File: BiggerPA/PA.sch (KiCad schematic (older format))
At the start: 105 parts, among them J1 Conn_Coaxial, J10 Conn_01x01, J2 Conn_01x02, J27 Conn_01x01, J28 Conn_01x01, J3 Conn_Coaxial, J4 Conn_01x02, J5 Conn_01x02, J6 Conn_01x01, J7 Conn_01x01, J8 Conn_01x01, J9 Conn_01x01, Q1 2N3906, Q10 IRF510N, Q11 IRF510N, Q12 IRF510N, Q13 IRF510N, Q14 IRF510N, Q15 IRF510N, Q18 TIP42, Q19 TIP42, Q2 IRF510N, Q20 TIP42, Q3 IRF510N, Q4 2N3906, Q5 TIP42, Q6 IRF510N, Q7 IRF510N, Q8 IRF510N, Q9 IRF510N, T1 Transformer_1P1Sdotted, T2 Transformer_1P1Sdotted, T3 Transformer_1P1Sdotted

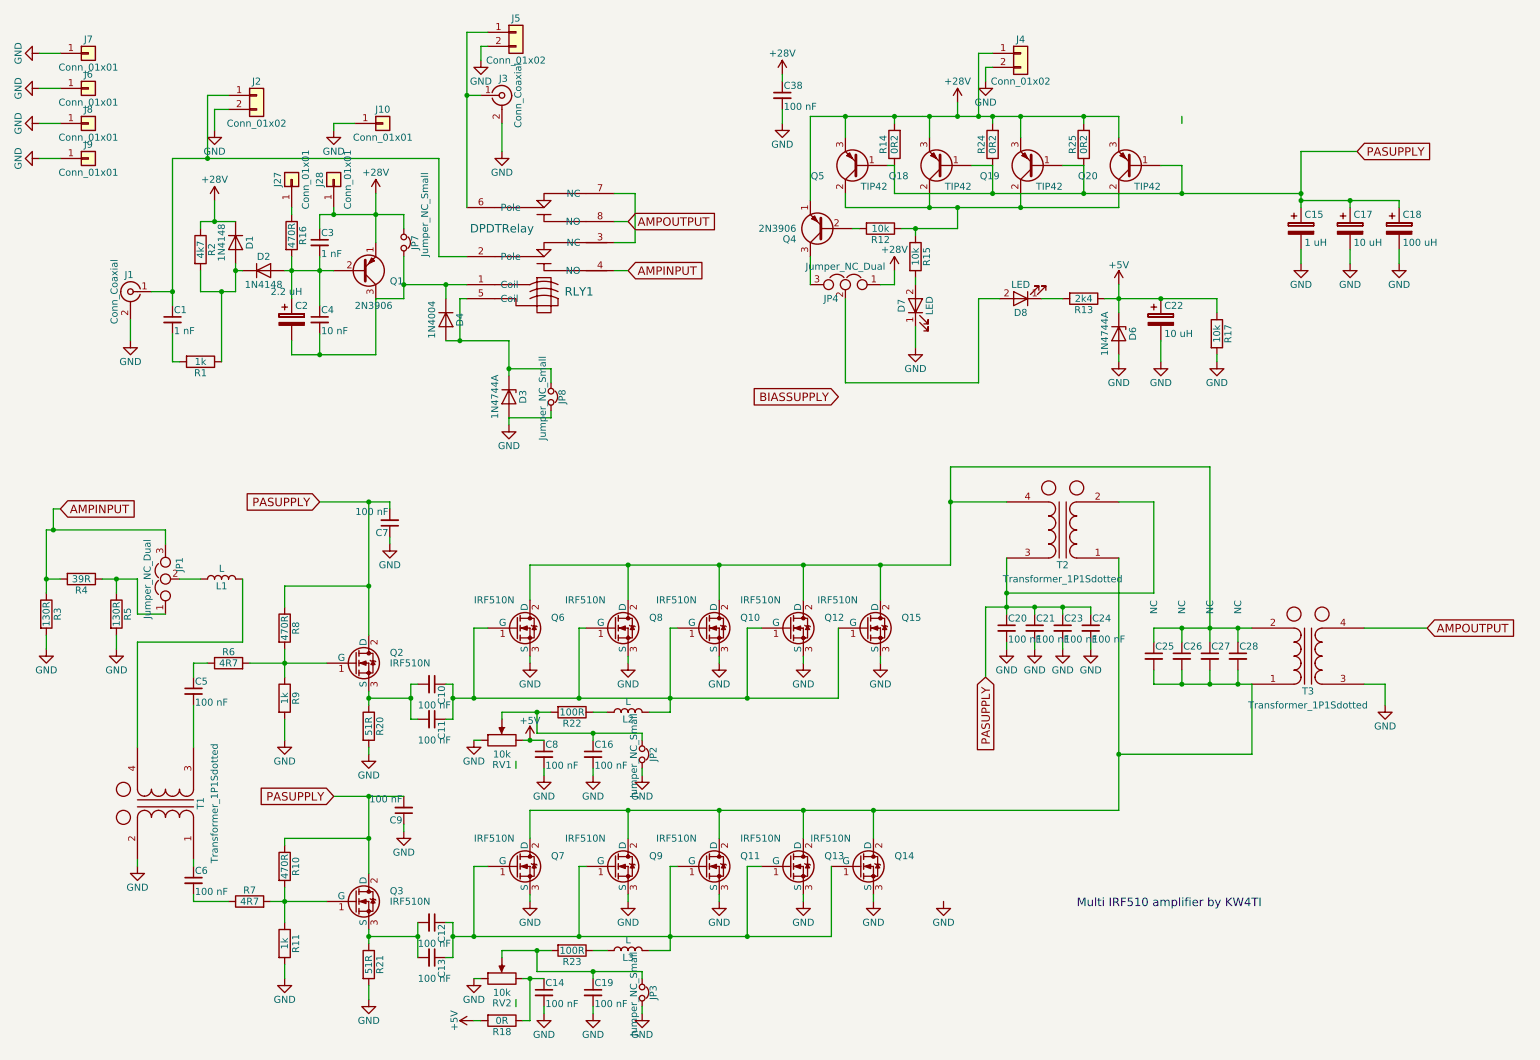
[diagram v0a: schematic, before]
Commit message: Added series inductor to gates
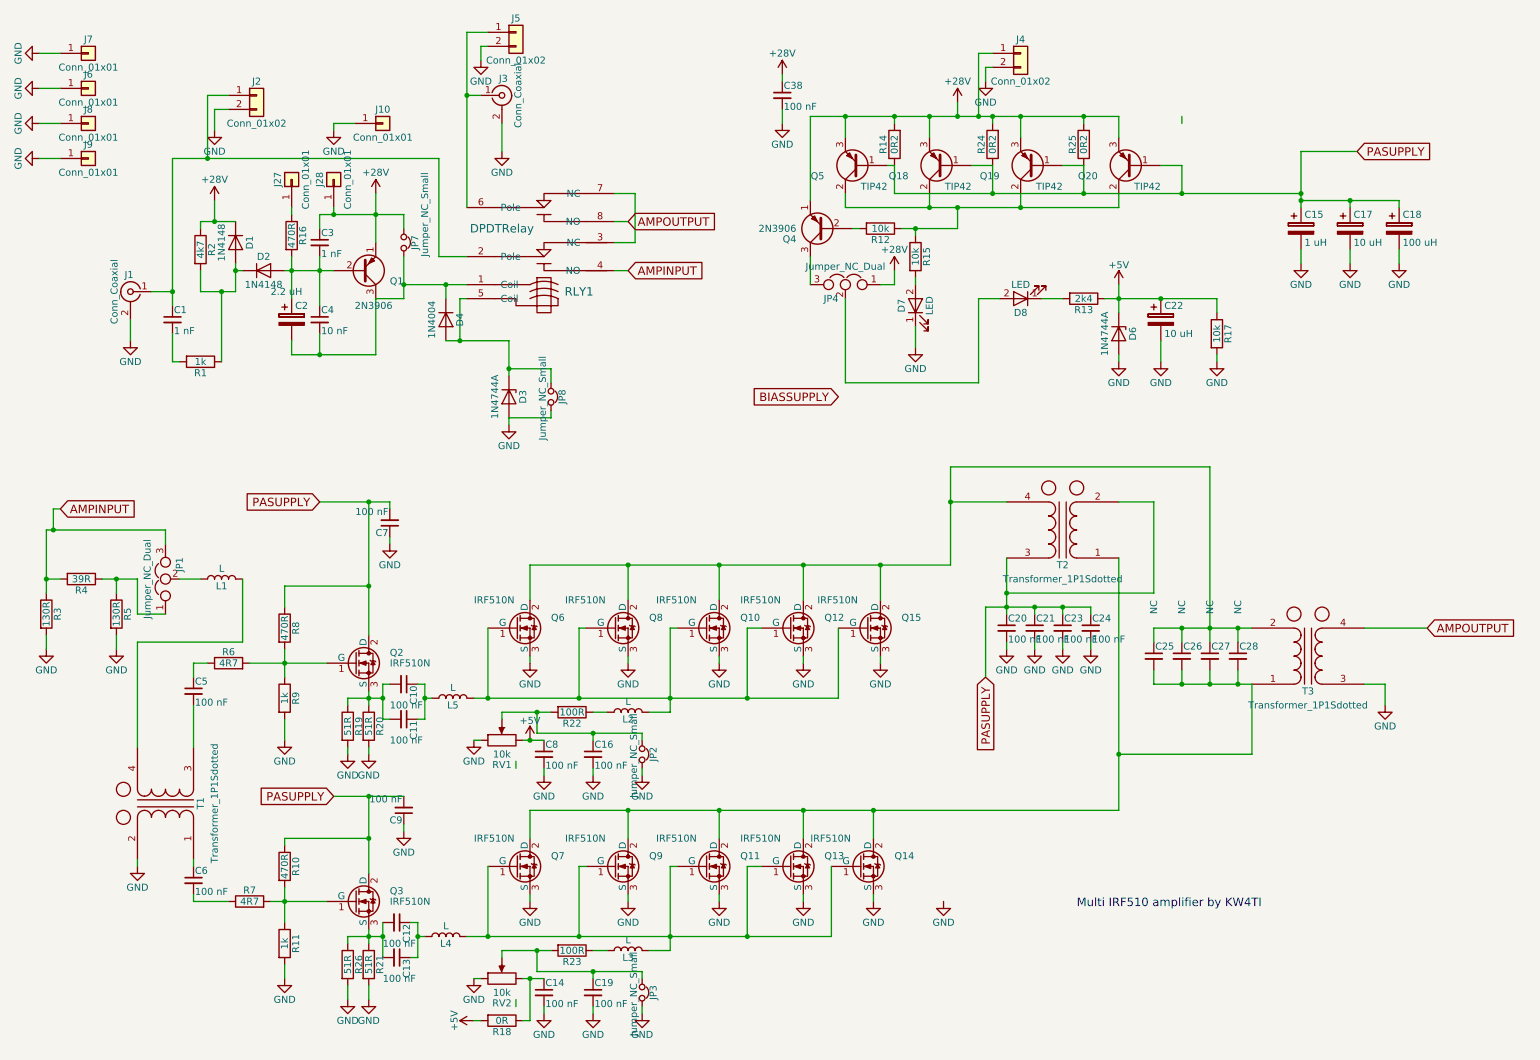
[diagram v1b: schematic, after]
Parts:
- added L4, L5: L, Inductors_THT:L_Axial_L6.6mm_D2.7mm_P10.16mm_Horizontal_Vishay_IM-2, symbol L
- added R19, R26: 51R, Resistors_THT:R_Axial_DIN0309_L9.0mm_D3.2mm_P12.70mm_Horizontal, symbol R
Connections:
- net GND: now also R19.2, R26.2
- net at C10.2, C11.2, Q2.3 (S)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: now also R19.1
- net at C12.2, C13.2, Q3.3 (S)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: now also R26.1
- net at L2.2, Q10.1 (G), Q12.1 (G)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: now also L5.2; no longer C10.1, C11.1
- net at L3.2, Q11.1 (G), Q13.1 (G)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: now also L4.2; no longer C12.1, C13.1
- new net: C10.1, C11.1, L5.1
- new net: C12.1, C13.1, L4.1
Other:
- moved on the sheet: C10, C11, C12, C13

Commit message: Added Filter
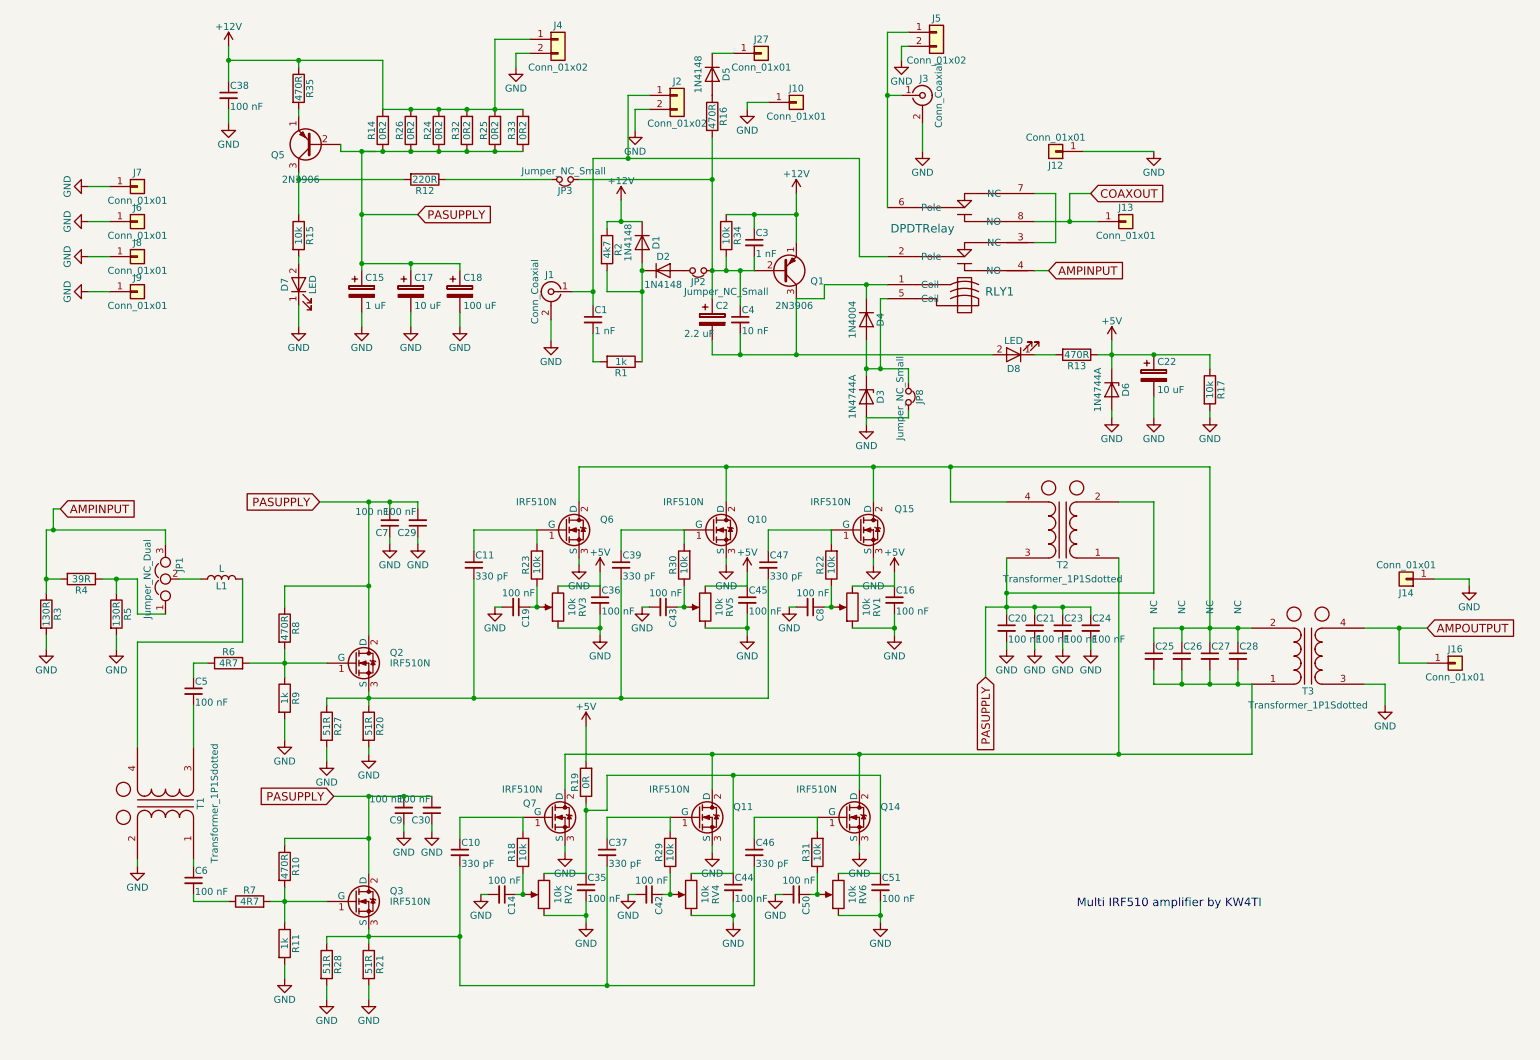
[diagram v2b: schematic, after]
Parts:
- removed C12, C13: 100 nF, Capacitors_THT:C_Disc_D5.0mm_W2.5mm_P5.00mm, symbol C_Small
- removed J28: Conn_01x01, Connectors:1pin, symbol Conn_01x01
- removed JP4: Jumper_NC_Dual, Pin_Headers:Pin_Header_Straight_1x03_Pitch2.54mm, symbol Jumper_NC_Dual
- removed JP7: Jumper_NC_Small, Pin_Headers:Pin_Header_Straight_1x02_Pitch2.54mm, symbol Jumper_NC_Small
- removed L2, L3, L4, L5: L, Inductors_THT:L_Axial_L6.6mm_D2.7mm_P10.16mm_Horizontal_Vishay_IM-2, symbol L
- removed Q12, Q13, Q8, Q9: IRF510N, PA:TO-220-3_Vertical_WithPads, symbol IRF540N
- removed Q18, Q19, Q20, Q5: TIP42, PA:TO-220-3_Vertical_WithPads, symbol TIP42
- removed Q4: 2N3906, TO_SOT_Packages_THT:TO-92_Molded_Narrow, symbol 2N3906
- added C29, C30, C35, C36, C42, C43, C44, C45, C50, C51: 100 nF, Capacitors_THT:C_Disc_D5.0mm_W2.5mm_P2.50mm, symbol C_Small
- added C37, C39, C46, C47: 330 pF, Capacitors_THT:C_Disc_D5.0mm_W2.5mm_P2.50mm, symbol C_Small
- added D5: 1N4148, Diodes_THT:D_DO-35_SOD27_P7.62mm_Horizontal, symbol D
- added J12, J13, J14, J16: Conn_01x01, Connectors:1pin, symbol Conn_01x01
- added Q5: 2N3906, TO_SOT_Packages_THT:TO-92_Molded_Narrow, symbol 2N3906
- added R27, R28: 51R, Resistors_THT:R_Axial_DIN0309_L9.0mm_D3.2mm_P12.70mm_Horizontal, symbol R
- added R29, R30, R31, R34: 10k, Resistors_THT:R_Axial_DIN0207_L6.3mm_D2.5mm_P7.62mm_Horizontal, symbol R
- added R32, R33: 0R2, Resistors_THT:R_Axial_DIN0411_L9.9mm_D3.6mm_P12.70mm_Horizontal, symbol R
- added R35: 470R, Resistors_THT:R_Axial_DIN0207_L6.3mm_D2.5mm_P7.62mm_Horizontal, symbol R
- added RV3, RV4, RV5, RV6: 10k, Potentiometers:Potentiometer_Trimmer_Bourns_3296W, symbol POT
- C10, C11: value 100 nF -> 330 pF; footprint Capacitors_THT:C_Disc_D5.0mm_W2.5mm_P5.00mm -> Capacitors_THT:C_Disc_D5.0mm_W2.5mm_P2.50mm
- C15: value 1 uH -> 1 uF
- C17, C22: value 10 uH -> 10 uF
- C18: value 100 uH -> 100 uF
- C2: value 2.2 uH -> 2.2 uF
- R12: value 10k -> 220R
- R13: value 2k4 -> 470R
- R18: value 0R -> 10k; footprint Resistors_THT:R_Axial_DIN0207_L6.3mm_D2.5mm_P10.16mm_Horizontal -> Resistors_THT:R_Axial_DIN0207_L6.3mm_D2.5mm_P7.62mm_Horizontal
- R19: value 51R -> 0R; footprint Resistors_THT:R_Axial_DIN0309_L9.0mm_D3.2mm_P12.70mm_Horizontal -> Resistors_THT:R_Axial_DIN0207_L6.3mm_D2.5mm_P7.62mm_Horizontal
- R22, R23: value 100R -> 10k; footprint Resistors_THT:R_Axial_DIN0207_L6.3mm_D2.5mm_P10.16mm_Horizontal -> Resistors_THT:R_Axial_DIN0207_L6.3mm_D2.5mm_P7.62mm_Horizontal
- R26: value 51R -> 0R2; footprint Resistors_THT:R_Axial_DIN0309_L9.0mm_D3.2mm_P12.70mm_Horizontal -> Resistors_THT:R_Axial_DIN0411_L9.9mm_D3.6mm_P12.70mm_Horizontal
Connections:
- net +5V: now also C16.1, R19.2, C36.1, C45.1, RV3.3, RV5.3; no longer C8.1, R18.2
- net AMPOUTPUT: now also J16.1 (Pin_1); no longer RLY1.8 (NO)
- net GND: now also C29.1, C30.1, C35.2, C36.2, C42.2, C43.2, C44.2, C45.2, C50.2, C51.2, J12.1 (Pin_1), J14.1 (Pin_1), R27.2, R28.2, RV3.1, RV4.1, RV5.1, RV6.1; no longer JP2.2, JP3.2, R19.2, R26.2
- net PASUPPLY: now also R26.1, C29.2, C30.2, Q5.2 (B), R32.1, R33.1
- net at C2.1, C3.2, C4.1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: now also JP2.1, JP3.1, R34.2; no longer D2.2 (A)
- net at C2.2, C4.2, D4.1 (K)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: now also D8.2 (A)
- net at C11.2, Q2.3 (S), R20.1: now also C39.2, C47.2, R27.1; no longer C10.2, R19.1
- net at Q3.3 (S), R21.1: now also C10.2, C37.2, C46.2, R28.1; no longer R26.1
- net at R12.2: now also R15.1, Q5.3 (C)
- net at R16.1: now also D5.2 (A); no longer J27.1 (Pin_1)
- net at R12.1: now also JP3.2; no longer R15.1
- net at C11.1: now also Q6.1 (G), R23.2; no longer C10.1
- net at R22.1: now also C8.1, RV1.2
- net at C14.1, R18.1: now also RV2.2; no longer RV2.3
- net at R23.1: now also C19.1, RV3.2
- net +28V renamed +12V
- net +12V: now also R26.2, R32.2, R33.2, R34.1, R35.1
- new net: D2.2 (A), JP2.2
- new net: D5.1 (K), J27.1 (Pin_1)
- new net: C47.1, Q15.1 (G), R22.2
- new net: C43.1, R30.1, RV5.2
- new net: C39.1, Q10.1 (G), R30.2
- new net: C50.1, R31.1, RV6.2
- new net: C46.1, Q14.1 (G), R31.2
- new net: C35.1, C44.1, C51.1, R19.1, RV2.3, RV4.3, RV6.3
- new net: C42.1, R29.1, RV4.2
- new net: C37.1, Q11.1 (G), R29.2
- new net: C10.1, Q7.1 (G), R18.2
- new net: Q5.1 (E), R35.2
- new net COAXOUT: J13.1 (Pin_1), RLY1.8 (NO)
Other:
- moved on the sheet: C1, C15, C16, C17, C18, C2, C22, C3, C38, C4, C8, D1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

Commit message: Changed to 7805 regulator
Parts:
- removed D6: 1N4744A, Diodes_THT:D_DO-41_SOD81_P7.62mm_Horizontal, symbol D_Zener
- removed R13: 470R, Resistors_THT:R_Axial_DIN0411_L9.9mm_D3.6mm_P12.70mm_Horizontal, symbol R
- added U1: LM7805_TO220, TO_SOT_Packages_THT:TO-220-3_Vertical, symbol LM7805_TO220
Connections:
- net +5V: now also U1.3 (VO)
- net GND: now also U1.2 (GND)
- net at D8.1 (K): now also U1.1 (VI)
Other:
- moved on the sheet: D8
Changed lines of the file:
@@
 $EndComp
 $Comp
-L R R13
-U 1 1 5C63AE6E
-P 8000 2850
-F 0 "R13" V 8080 2850 50  0000 C CNN
-F 1 "470R" V 8000 2850 50  0000 C CNN
-F 2 "Resistors_THT:R_Axial_DIN0411_L9.9mm_D3.6mm_P12.70mm_Horizontal" V 7930 2850 50  0001 C CNN
-F 3 "" H 8000 2850 50  0001 C CNN
-	1    8000 2850
-	0    1    1    0
-$EndComp
-$Comp
-L D_Zener D6
-U 1 1 5C63B217
-P 8250 3100
-F 0 "D6" H 8250 3200 50  0000 C CNN
-F 1 "1N4744A" H 8250 3000 50  0000 C CNN
-F 2 "Diodes_THT:D_DO-41_SOD81_P7.62mm_Horizontal" H 8250 3100 50  0001 C CNN
-F 3 "" H 8250 3100 50  0001 C CNN
-	1    8250 3100
-	0    1    1    0
-$EndComp
-$Comp
-L GND #PWR60
-U 1 1 5C63B4B9
-P 8250 3300
-F 0 "#PWR60" H 8250 3050 50  0001 C CNN
-F 1 "GND" H 8250 3150 50  0000 C CNN
-F 2 "" H 8250 3300 50  0001 C CNN
-F 3 "" H 8250 3300 50  0001 C CNN
-	1    8250 3300
-	1    0    0    -1
-$EndComp
-$Comp
-L +5V #PWR59
+L +5V #PWR60
 U 1 1 5C63B9B6
 P 8250 2750
-F 0 "#PWR59" H 8250 2600 50  0001 C CNN
+F 0 "#PWR60" H 8250 2600 50  0001 C CNN
 F 1 "+5V" H 8250 2890 50  0000 C CNN
 F 2 "" H 8250 2750 50  0001 C CNN
@@
 L LED D8
 U 1 1 5CF37149
-P 7550 2850
-F 0 "D8" H 7550 2950 50  0000 C CNN
-F 1 "LED" H 7550 2750 50  0000 C CNN
-F 2 "LEDs:LED_D3.0mm" H 7550 2850 50  0001 C CNN
-F 3 "" H 7550 2850 50  0001 C CNN
-	1    7550 2850
+P 7000 2850
+F 0 "D8" H 7000 2950 50  0000 C CNN
+F 1 "LED" H 7000 2750 50  0000 C CNN
+F 2 "LEDs:LED_D3.0mm" H 7000 2850 50  0001 C CNN
+F 3 "" H 7000 2850 50  0001 C CNN
+	1    7000 2850
 	-1   0    0    1
 $EndComp
@@
 $EndComp
 $Comp
-L GND #PWR56
+L GND #PWR57
 U 1 1 5D171E1D
 P 7700 4950
-F 0 "#PWR56" H 7700 4700 50  0001 C CNN
+F 0 "#PWR57" H 7700 4700 50  0001 C CNN
 F 1 "GND" H 7700 4800 50  0000 C CNN
 F 2 "" H 7700 4950 50  0001 C CNN
@@
 $EndComp
 $Comp
-L GND #PWR57
+L GND #PWR58
 U 1 1 5D172120
 P 7900 4950
-F 0 "#PWR57" H 7900 4700 50  0001 C CNN
+F 0 "#PWR58" H 7900 4700 50  0001 C CNN
 F 1 "GND" H 7900 4800 50  0000 C CNN
 F 2 "" H 7900 4950 50  0001 C CNN
@@
 $EndComp
 $Comp
-L GND #PWR58
+L GND #PWR59
 U 1 1 5D172424
 P 8100 4950
-F 0 "#PWR58" H 8100 4700 50  0001 C CNN
+F 0 "#PWR59" H 8100 4700 50  0001 C CNN
 F 1 "GND" H 8100 4800 50  0000 C CNN
 F 2 "" H 8100 4950 50  0001 C CNN
@@
 	3600 2200 3600 2250
 Wire Wire Line
-	8250 2750 8250 2950
-Wire Wire Line
-	8150 2850 8950 2850
-Wire Wire Line
-	8250 3300 8250 3250
+	8250 2750 8250 2850
+Wire Wire Line
+	7850 2850 8950 2850
 Connection ~ 8250 2850
 Wire Wire Line
@@
 	950  2400 1100 2400
 Wire Wire Line
-	7700 2850 7850 2850
+	7150 2850 7250 2850
 Wire Wire Line
 	2450 2150 2450 2200
@@
 	9250 5200 9250 5700
 Wire Wire Line
-	9250 5700 4350 5700
+	4350 5700 9250 5700
 Connection ~ 8300 5700
 Wire Wire Line
@@
 	5400 2750 5400 2850
 Wire Wire Line
-	5400 2850 7400 2850
+	5400 2850 6850 2850
 Connection ~ 6000 1850
 Connection ~ 5400 2250
@@
 Wire Wire Line
 	2450 1100 2450 1150
+$Comp
+L LM7805_TO220 U1
+U 1 1 5D1A1436
+P 7550 2850
+F 0 "U1" H 7400 2975 50  0000 C CNN
+F 1 "LM7805_TO220" H 7550 2975 50  0000 L CNN
+F 2 "TO_SOT_Packages_THT:TO-220-3_Vertical" H 7550 3075 50  0001 C CIN
+F 3 "" H 7550 2800 50  0001 C CNN
+	1    7550 2850
+	1    0    0    -1
+$EndComp
+$Comp
+L GND #PWR56
+U 1 1 5D1A1FC5
+P 7550 3300
+F 0 "#PWR56" H 7550 3050 50  0001 C CNN
+F 1 "GND" H 7550 3150 50  0000 C CNN
+F 2 "" H 7550 3300 50  0001 C CNN
+F 3 "" H 7550 3300 50  0001 C CNN
+	1    7550 3300
+	1    0    0    -1
+$EndComp
+Wire Wire Line
+	7550 3150 7550 3300
 $EndSCHEMATC
